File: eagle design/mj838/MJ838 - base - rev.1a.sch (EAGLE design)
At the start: 11 parts, among them J1 Vdc, J2 Dynamo, J3 CAN, J4 Battery, J5 FTSH-107-01-L-DV-K-A

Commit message: in mj8x8.h: - prepared for SPI
in mj838.c/.h:
- preparation for sd card logger functionality
- adapted for I2C FeRAM IC change
- conversion to integer math:
-- scaled up wheel circumferences from floating point meters to integer millimeters: 2.350 became 2350
-- converted data members to integer
-- adapted algorithm to do computation in integer arithmetic and not floating point
- prepared for SPI
- removed PowerMonitorPower_Pin (was PB8) and created definition for general PB8_Pin GPIO
- started transfer from pac1952 objects towards ina219 objects

in adxl367.c/.h:
- continued driver development
- defined register addresses and sizes
- misc comment corrections
- added template for device driver

in autocharge.c:
- corrected speed value for SSR control
- fixed premature power off bug in _Do() where __AutoCharge._LEDDriver->Power() was called wrongly
- conversion to integer math:
-- converted data members to integer
-- adapted algorithm to do computation in integer arithmetic and not floating point
- started transfer from pac1952 objects towards ina219 objects
- modified code so that adjustable load does blink/not blink depending on speed

in zerocross.h, mj838_zerocross.c:
- added define to turn off zero cross frequency change rate calculation
- conversion to integer math:
-- converted data members to integer
-- adapted algorithm to do computation in integer arithmetic and not floating point
- moved __ZeroCross location to .data

in fm24cl.c./h:
- modified/renamed old mb85rc driver to work with new IC

in autodrive.c:
- in autodrive_ctor() added call to measure temperature/humidity at initialization

in i2c.c:
- as a temporary solution (until 1k pull-up resistors arrive), converted to pooling transfer functions and a 100kHz data transfer rate and built-in stm32 pull-up resistors
- activated high speed I2C, turned off internal pullups

in spi.c/.h:
- work on init function

in dac121c081.c:
- removed double declaration of __DAC121C081 object

in ina219.c:
- continued wo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
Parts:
- MARKER2: value (none) -> 4 Layer marker
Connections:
- net VDC: now also CONN2.61, CONN2.62, CONN2.63, CONN2.64, CONN2.65, CONN2.66
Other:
- note added: "mj838 - Čos - base HW rev.1a"
- note removed: "mj838 - Čos - base HW rev.11"

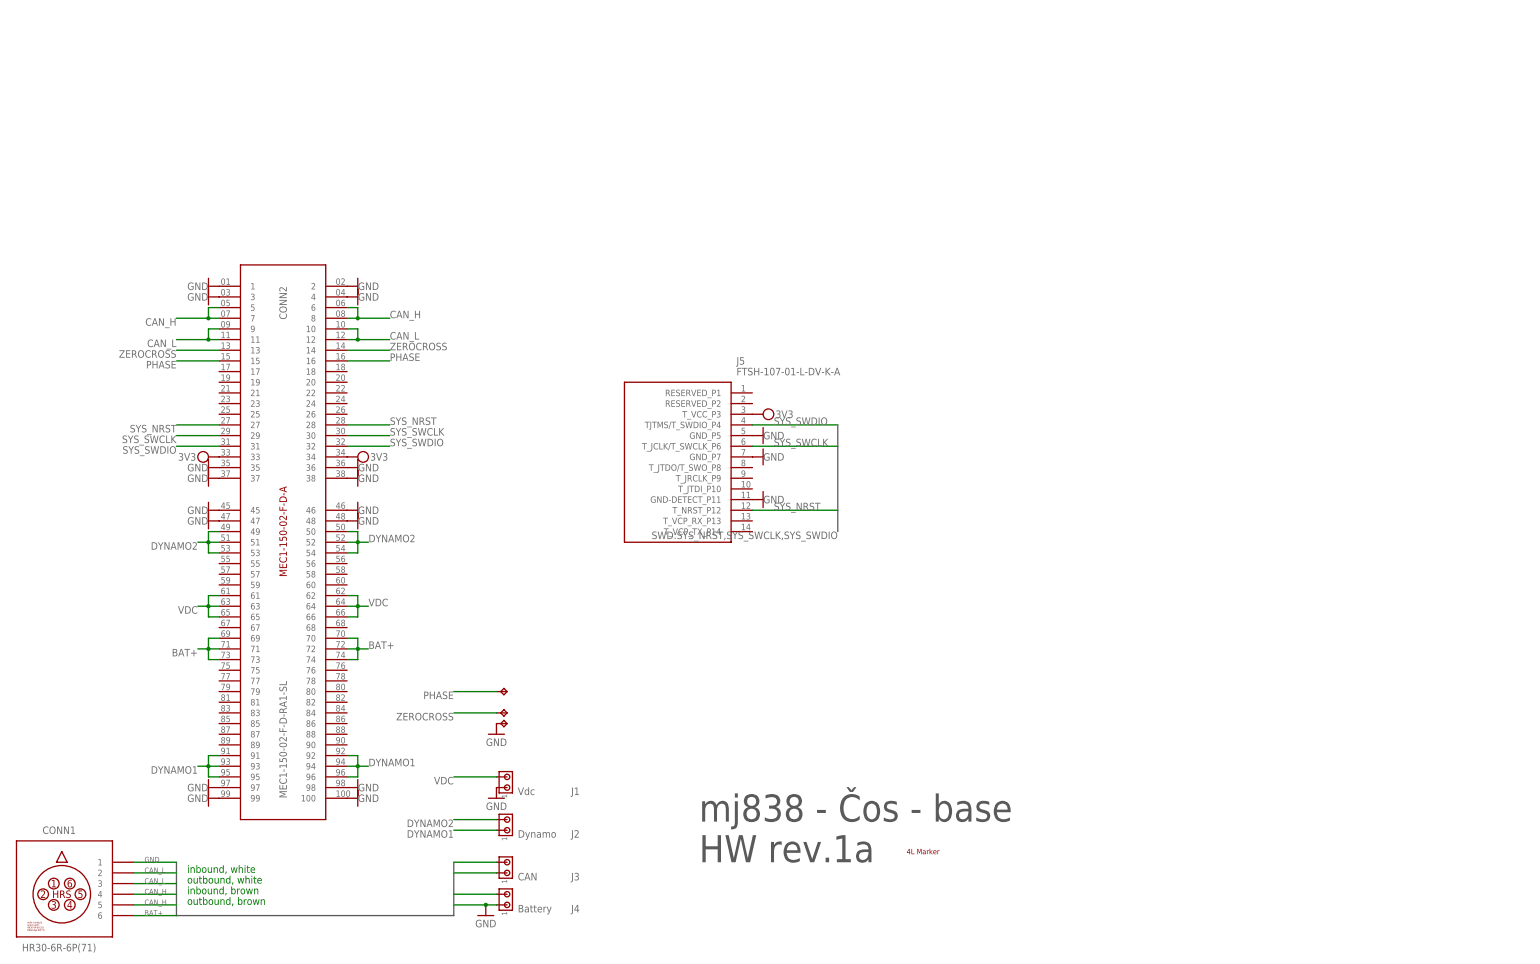
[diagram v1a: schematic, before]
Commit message: finished HR30_6R_6PD(71) - FFC layout.brd & .sch this item allows for FFC connectivity between the base board and external connectors. the FFC has a pitch-out of 1mm (FFC width of 11mm) and mates with a HR30_6R_6PD(71) TH receptacle and a Samtecc FC1-10-02-T-WT FFC connector.
finished MJ838 - base - rev.1a.brd
this item is an improved version of the original base board.
it now can accept either the RA or straight version of the MEC1-150-02 card edge connector.
this board can be connected via wires or via the above HR30_6R_6PD(71) - FFC layout.brd.
for wired connection terminal blocks are used, for FFC connection a Samtec FC1-10-02-T-WT is used.
!!! these rev.1 base boards are NOT COMPATIBLE with earlier boards !!!

finished MJ838 - rev.1c.brd & .sch
this item is the next revision of the MJ838 device.
it follows a dual-device design started with rev.1b - the schematic/board are developed to support both mj838 and mj000 devices, depending on which firmware is loaded and which components are populated.
major improvements for mj838/mj000 in respect to rev.1b:
- far more powerful MCU (STM32L4P5CGU6) - more flash/ram, floating point, SDMMC, QSPI
- improved zerocross detection via TLV6703DDCR's internal refernece voltage
- addition of numerous TVS protection elements (SWD, ZC & phase signals, SDMMC interface)
- addition of the ADXL367 - Accelerometer for improved motion detection
- addition of QSPI for MRAM storage
- switch from SPI to SDMMC for interfacing SD Card storage
- addition of RN4678 bluetooth module (via UART) for wireless data transfer
- improved routing of MJ8x8 power bus, application load lines to card edge (and into base board) so that prod<->dev card swap is far easier
- addition of NFET controlled application/adjustable load switch

added old boards for reference; their name prefix is "reference - *"
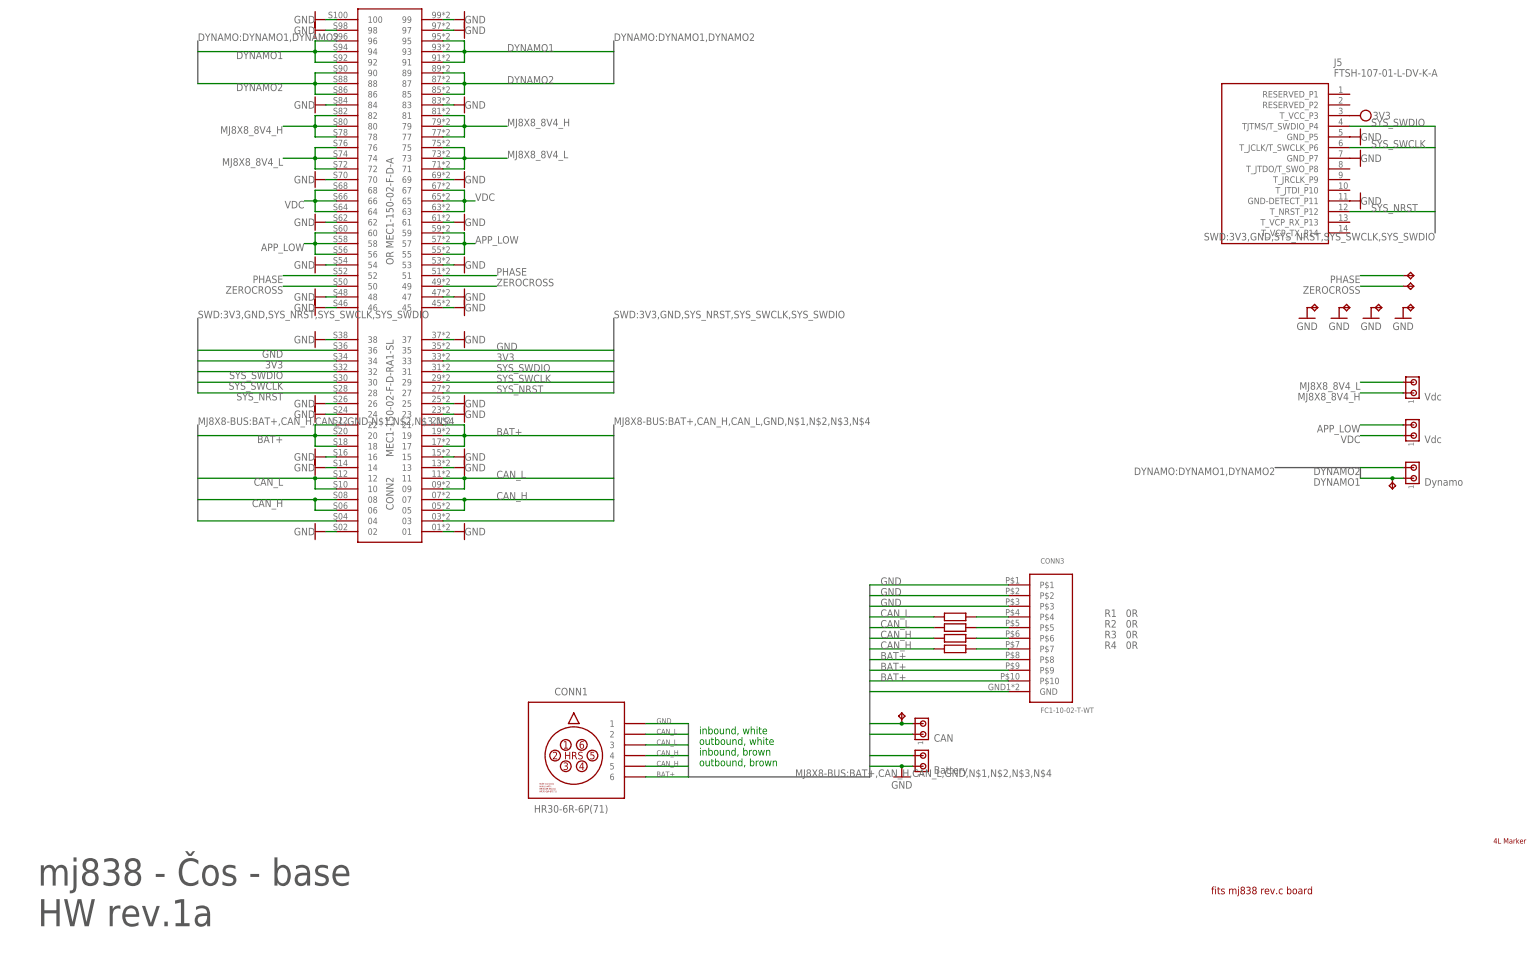
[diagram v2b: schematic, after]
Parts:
- removed J1: Vdc, con-amp:MTA02-100
- added CONN3: FC1-10-02-T-WT, FC1-10-02-T - FFC Connector:FC1-10-02-T-FFC_CONNECTOR
- added J6, J7: Vdc, con-amp:MTA02-100
- added R1, R2, R3, R4: 0R, rcl:R-EU_R0402
- added TP4, TP5, TP6, TP8, TP9: TPPAD1-13, testpad:TPPAD1-13
- CONN2: device Samtec MEC1 - Card Edge Connector:MEC1-150-2-F-D-RA -> MEC1-150-X-X-D-RA1-SL-X:MEC1-150-02-F-D-AMEC1-150-02-F-D-COMBINED
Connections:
- new net APP_LOW: CONN2.55, CONN2.56, CONN2.57, CONN2.58, CONN2.59, CONN2.60, J7.2
- new net MJ8X8_8V4_H: CONN2.77, CONN2.78, CONN2.79, CONN2.80, CONN2.81, CONN2.82, J6.1
- new net MJ8X8_8V4_L: CONN2.71, CONN2.72, CONN2.73, CONN2.74, CONN2.75, CONN2.76, J6.2
- new net N$1: CONN3.P$4, R1.2
- new net N$2: CONN3.P$5, R2.2
- new net N$3: CONN3.P$6, R3.2
- new net N$4: CONN3.P$7, R4.2
- net BAT+: now also CONN2.17, CONN2.18, CONN2.19, CONN2.20, CONN2.21, CONN2.22, CONN3.P$10, CONN3.P$8, CONN3.P$9; no longer CONN2.69, CONN2.70, CONN2.71, CONN2.72, CONN2.73, CONN2.74
- net CAN_H: now also CONN2.05, CONN2.06, CONN2.07, CONN2.08, R3.1, R4.1, TP6.TP; no longer CONN2.5, CONN2.6, CONN2.7, CONN2.8
- net CAN_L: now also CONN2.09, R1.1, R2.1; no longer CONN2.9
- net DYNAMO1: now also TP5.TP
- net DYNAMO2: now also CONN2.85, CONN2.86, CONN2.87, CONN2.88, CONN2.89, CONN2.90; no longer CONN2.49, CONN2.50, CONN2.51, CONN2.52, CONN2.53, CONN2.54
- net GND: now also CONN2.01, CONN2.02, CONN2.03, CONN2.04, CONN2.13, CONN2.14, CONN2.15, CONN2.16, CONN2.23, CONN2.24, CONN2.25, CONN2.26, CONN2.53, CONN2.54, CONN2.61, CONN2.62, CONN2.69, CONN2.70, CONN2.83, CONN2.84, CONN3.GND, CONN3.P$1, CONN3.P$2, CONN3.P$3, TP4.TP, TP8.TP, TP9.TP; no longer CONN2.1, CONN2.2, CONN2.3, CONN2.4, J1.1
- net PHASE: now also CONN2.51, CONN2.52; no longer CONN2.15, CONN2.16
- net VDC: now also CONN2.67, CONN2.68, J7.1; no longer CONN2.61, CONN2.62, J1.2
- net ZEROCROSS: now also CONN2.49, CONN2.50; no longer CONN2.13, CONN2.14
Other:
- note added: "OR MEC1-150-02-F-D-A"
- note added: "fits mj838 rev.c board"
- moved on the sheet: CONN1, J5
